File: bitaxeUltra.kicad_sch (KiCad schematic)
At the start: 16 parts, among them J1 54-00164

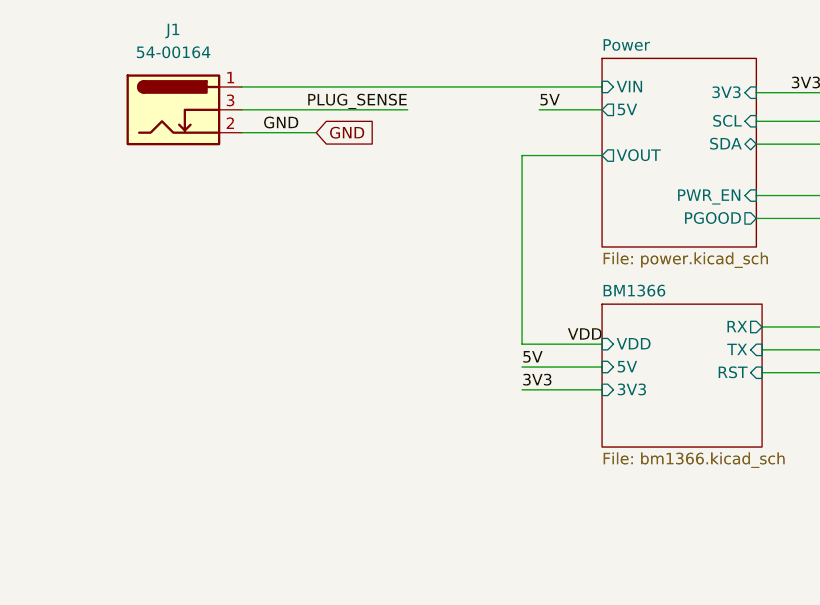
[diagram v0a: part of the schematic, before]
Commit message: Finish LED layout. Can pass to factory for prototype test
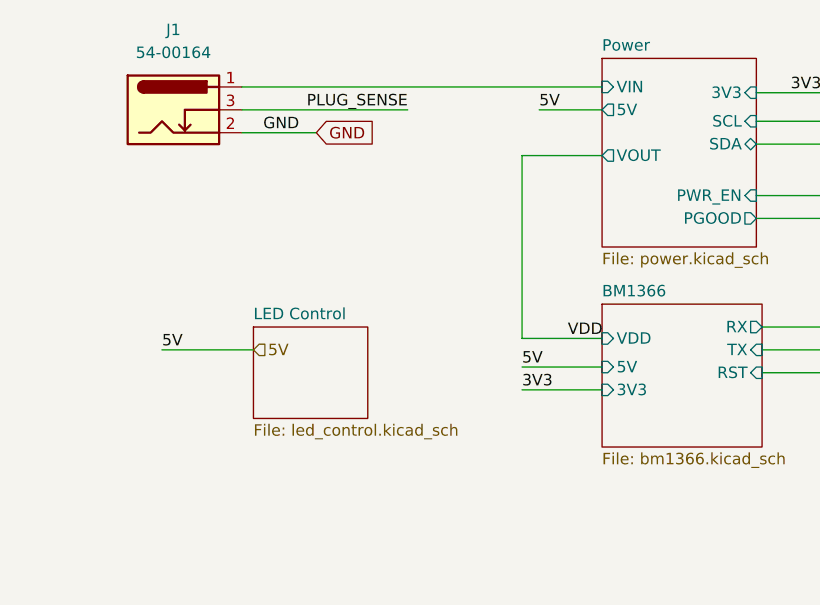
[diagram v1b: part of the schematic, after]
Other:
- added sheet LED Control (led_control.kicad_sch)
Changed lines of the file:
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@@
+    (stroke (width 0) (type default))
+  )
+  (wire (pts (xy 63.5 72.39) (xy 73.66 72.39))
     (stroke (width 0) (type default))
   )
@@
     (stroke (width 0) (type default))
   )
-  (wire (pts (xy 103.505 71.755) (xy 103.505 50.8))
+  (wire (pts (xy 103.505 71.12) (xy 103.505 50.8))
     (stroke (width 0) (type default))
   )
@@
     (stroke (width 0) (type default))
   )
-  (wire (pts (xy 112.395 71.755) (xy 103.505 71.755))
+  (wire (pts (xy 112.395 71.12) (xy 103.505 71.12))
     (stroke (width 0) (type default))
   )
@@
     (effects (font (size 1.27 1.27)) (justify right bottom))
   )
+  (label "5V" (at 63.5 72.39 0) (fields_autoplaced)
+    (effects (font (size 1.27 1.27)) (justify left bottom))
+  )
   (label "VDD" (at 165.735 83.185 0) (fields_autoplaced)
     (effects (font (size 1.27 1.27)) (justify left bottom))
@@
     (effects (font (size 1.27 1.27)) (justify left bottom))
   )
-  (label "VDD" (at 108.585 71.755 0) (fields_autoplaced)
+  (label "VDD" (at 108.585 71.12 0) (fields_autoplaced)
     (effects (font (size 1.27 1.27)) (justify left bottom))
   )
@@
     )
   )
+  (hierarchical_label "5V" (shape input) (at 73.66 72.39 0) (fields_autoplaced)
+    (effects (font (size 1.27 1.27)) (justify left))
+  )
   (symbol (lib_id "Mechanical:Fiducial") (at 90.805 177.165 0) (unit 1)
     (in_bom no) (on_board yes) (dnp no) (fields_autoplaced)
@@
       (effects (font (size 1.27 1.27)) hide)
     )
-    (property "Datasheet" "https://tensility.s3.amazonaws.com/uploads/pdffiles/54-00164.pdf?X-Amz-Expires=600&X-Amz-Date=20231120T033415Z&X-Amz-Algorithm=AWS4-HMAC-SHA256&X-Amz-Credential=AKIAIS2S4WRDQDSWDRZQ%2F20231120%2Fus-west-2%2Fs3%2Faws4_request&X-Amz-SignedHeaders=host&X-Amz-Signature=0ec7ce6b9e4957ccc83a05eb1138fede41cc8592648d2aac3c65914c1c151ca7" (at 66.04 46.736 0)
+    (property "Datasheet" "~" (at 66.04 46.736 0)
       (effects (font (size 1.27 1.27)) hide)
     )
@@
           (reference "U3") (unit 1)
         )
+      )
+    )
+  )
+  (sheet (at 73.66 69.85) (size 12.7 10.16) (fields_autoplaced)
+    (stroke (width 0.1524) (type solid))
+    (fill (color 0 0 0 0.0000))
+    (property "Sheetname" "LED Control" (at 73.66 69.1384 0)
+      (effects (font (size 1.27 1.27)) (justify left bottom))
+    )
+    (property "Sheetfile" "led_control.kicad_sch" (at 73.66 80.5946 0)
+      (effects (font (size 1.27 1.27)) (justify left top))
+    )
+    (instances
+      (project "bitaxeUltra"
+        (path "/e63e39d7-6ac0-4ffd-8aa3-1841a4541b55" (page "6"))
       )
     )
@@
       (effects (font (size 1.27 1.27)) (justify left))
     )
-    (pin "VDD" input (at 112.395 71.755 180)
-      (effects (font (size 1.27 1.27)) (justify left))
-    )
+    (pin "VDD" input (at 112.395 71.12 180)
+      (effects (font (size 1.27 1.27)) (justify left))
+    )
